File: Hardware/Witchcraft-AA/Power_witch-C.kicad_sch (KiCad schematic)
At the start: 12 parts, among them J3 Conn_Power_Coax_IBM_hanging_M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, J4 Molex_0015913074, J5 Conn_01x02_Socket, U1 Z1 extreme, U2 LM26420-Q1xx-xxxx

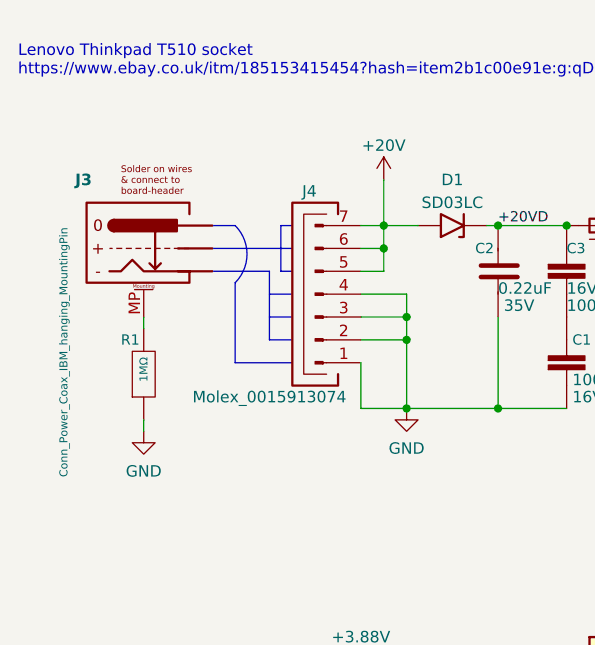
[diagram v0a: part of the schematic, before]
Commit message: Started working on custom buttons for the shell.
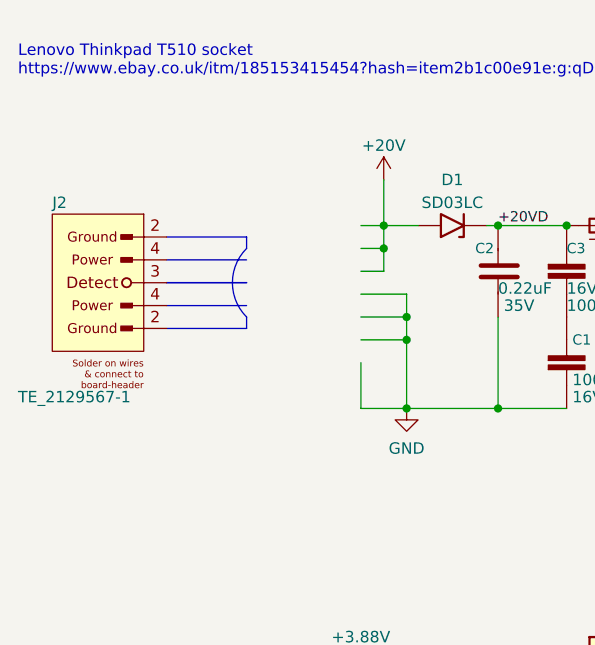
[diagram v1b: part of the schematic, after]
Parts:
- removed J3: Conn_Power_Coax_IBM_hanging_MountingPin, LRJ:Jack_IBM_Coax_Power_5.55x7.5mm_Hanging, symbol LRJ-parts:Conn_Power_Coax_hanging_MountingPin
- removed J4: Molex_0015913074, LRJ:Molex_70634_15913074_1x07-2MP_P2.54mm_Vertical, symbol LRJ-parts:Molex_0015913074
- removed R1: R_ERJ-3GEYJ105V, Resistor_SMD:R_0603_1608Metric, symbol LRJ-parts:R_ERJ-3GEYJ105V
- added J2: TE_2129567-1, LRJ:TE_2129567-1, symbol LRJ-parts:TE_2129567-1

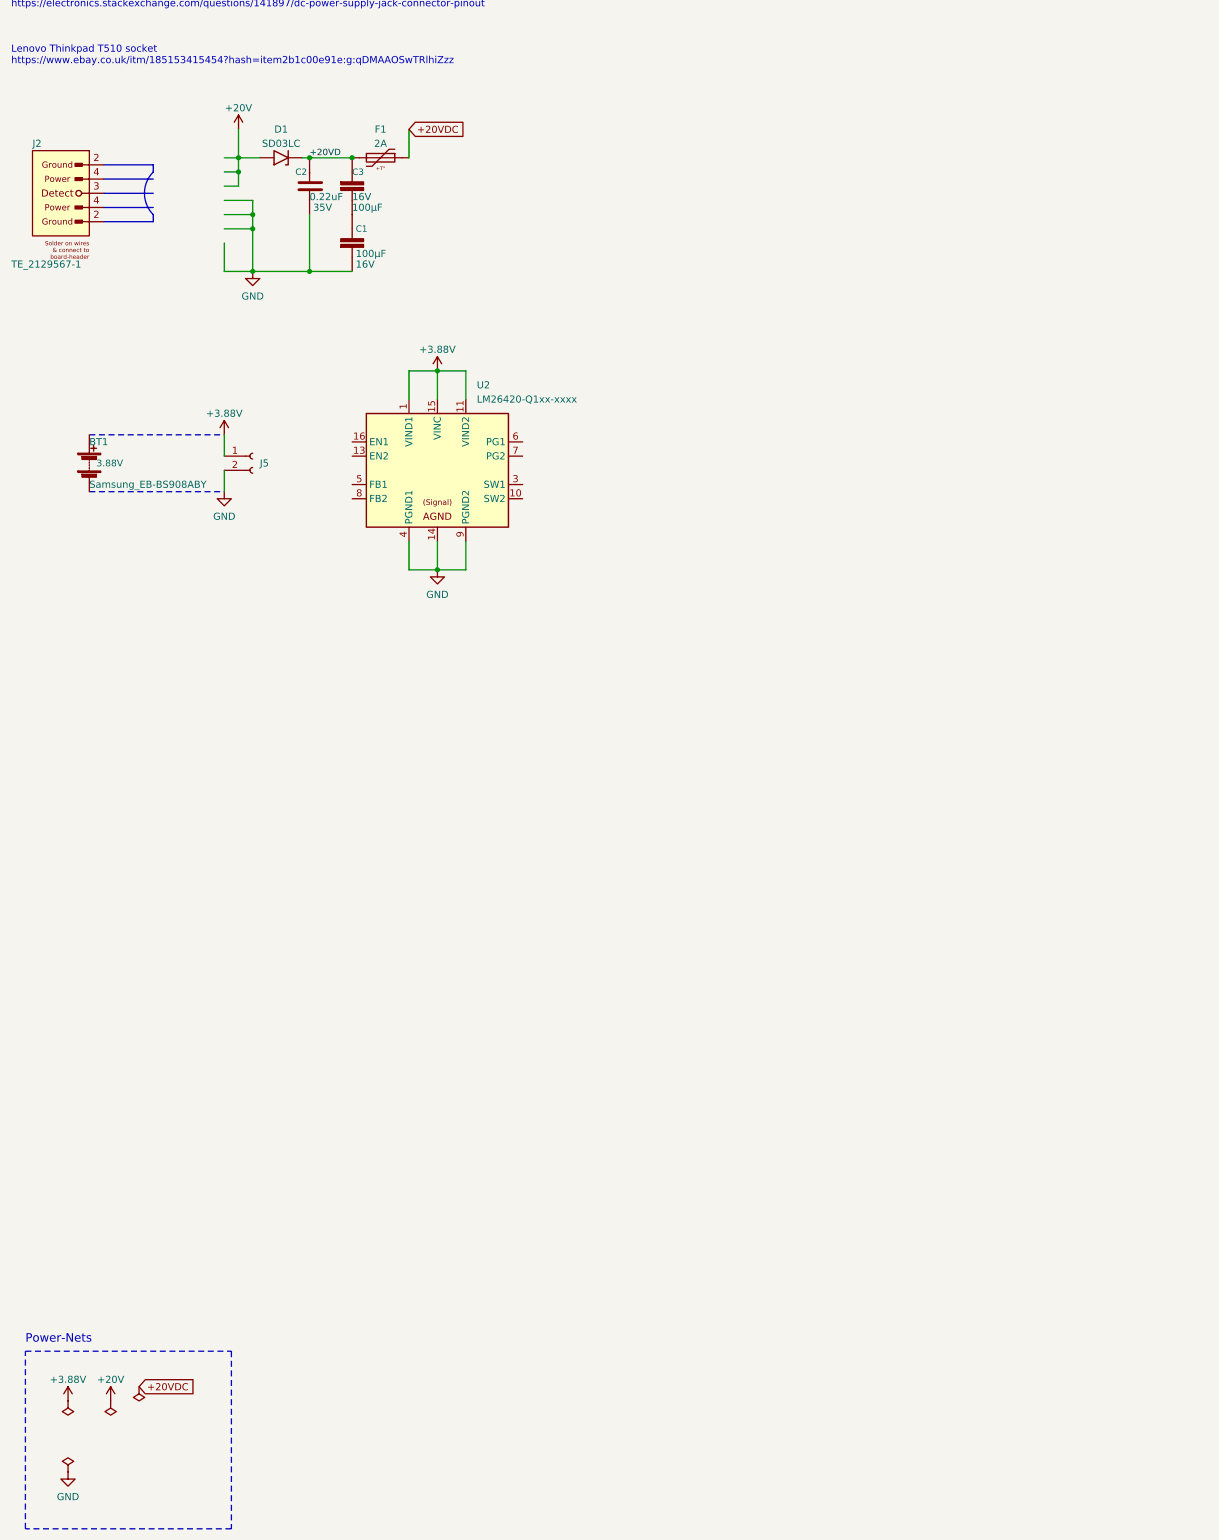
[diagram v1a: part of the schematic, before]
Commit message: added a mag-lev switch assembly to the shell, and started adding button-switches to the schematic.
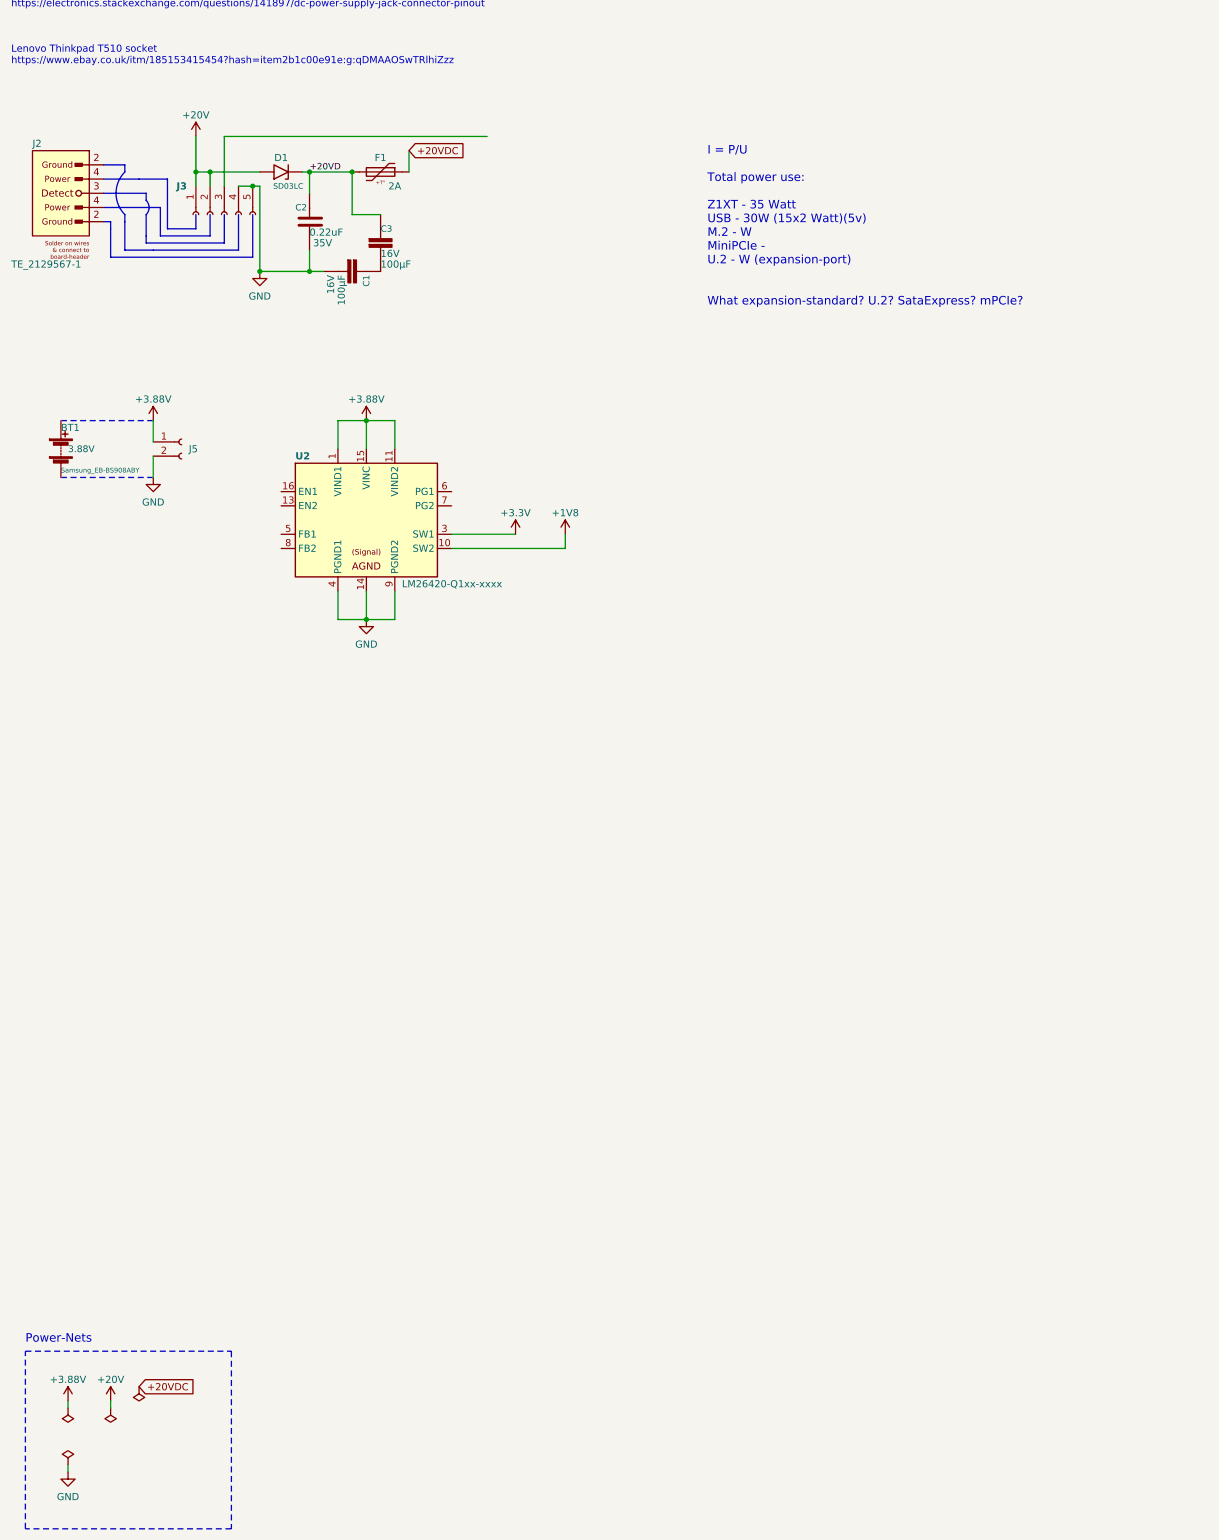
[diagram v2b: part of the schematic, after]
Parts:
- added J3: Conn_01x05_Socket, Connector_PinHeader_1.27mm:PinHeader_1x05_P1.27mm_Vertical_SMD_Pin1Left, symbol Connector:Conn_01x05_Socket
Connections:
- net +20V: now also J3.1 (Pin_1), J3.2 (Pin_2)
- net GND: now also J3.4 (Pin_4), J3.5 (Pin_5)
- net +1V8: now reaches U2.10 (SW2)
- net +3.3V: now reaches U2.3 (SW1)
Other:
- note added: "I = P/U Total power use: Z1XT - 35 Watt USB - 30W (15x2 Watt)(5v) M.2 - W MiniPCIe - U.2 - W (expansion-port) What expansion-standard? U.2? SataExpress? mPCIe?"
- moved on the sheet: BT1, C1, C2, C3, D1, F1, J5, U2

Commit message: Some chances to start/rectangle-buttons in mech, and startedmaking the M.2 ports.
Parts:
- added U3, U4: K3LKCKC0BM, LRJ:SAMSUNG_FBGA-315_12x14mm_Layout23x23_P0.5mmP0.65mm, symbol LRJ-parts:K3LKCKC0BM-MFCP
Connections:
- net GND: now also U3.B12 (VSS), U3.B2 (VSS), U3.B5 (VSS), U3.B6 (VSS), U3.C3 (VSS), U3.C5 (VSS), U3.C6 (VSS), U3.D12 (VSS), U3.D3 (VSS), U3.E4 (VSS), U3.E5 (VSS), U3.E6 (VSS), U3.F12 (VSS), U3.F4 (VSS), U3.F5 (VSS), U3.F6 (VSS), U3.G3 (VSS), U3.G4 (VSS), U3.G6 (VSS), U3.G9 (VSS), U3.H10 (VSS), U3.H2 (VSS), U3.J12 (VSS), U3.J4 (VSS), U3.K10 (VSS), U3.K2 (VSS), U3.L6 (VSS), U3.L9 (VSS), U3.M12 (VSS), U3.M4 (VSS), U3.M5 (VSS), U3.M6 (VSS), U3.N4 (VSS), U3.N5 (VSS), U3.N6 (VSS), U3.P12 (VSS), U3.P3 (VSS), U3.R4 (VSS), U3.R5 (VSS), U3.R6 (VSS), U3.T12 (VSS), U3.T2 (VSS), U3.T3 (VSS), U3.T4 (VSS), U3.T5 (VSS), U3.T6 (VSS), U4.B12 (VSS), U4.B2 (VSS), U4.B5 (VSS), U4.B6 (VSS), U4.C3 (VSS), U4.C5 (VSS), U4.C6 (VSS), U4.D12 (VSS), U4.D3 (VSS), U4.E4 (VSS), U4.E5 (VSS), U4.E6 (VSS), U4.F12 (VSS), U4.F4 (VSS), U4.F5 (VSS), U4.F6 (VSS), U4.G3 (VSS), U4.G4 (VSS), U4.G6 (VSS), U4.G9 (VSS), U4.H10 (VSS), U4.H2 (VSS), U4.J12 (VSS), U4.J4 (VSS), U4.K10 (VSS), U4.K2 (VSS), U4.L6 (VSS), U4.L9 (VSS), U4.M12 (VSS), U4.M4 (VSS), U4.M5 (VSS), U4.M6 (VSS), U4.N4 (VSS), U4.N5 (VSS), U4.N6 (VSS), U4.P12 (VSS), U4.P3 (VSS), U4.R4 (VSS), U4.R5 (VSS), U4.R6 (VSS), U4.T12 (VSS), U4.T2 (VSS), U4.T3 (VSS), U4.T4 (VSS), U4.T5 (VSS), U4.T6 (VSS)
- net Power_Detect: now reaches J3.3 (Pin_3)
- new net: U4.A10 (VDD1), U4.A3 (VDD1), U4.A4 (VDD1), U4.A5 (VDD1), U4.A6 (VDD1), U4.U10 (VDD1), U4.U3 (VDD1), U4.U4 (VDD1), U4.U5 (VDD1), U4.U6 (VDD1)
- new net: U4.A11 (VDDQ), U4.C12 (VDDQ), U4.E12 (VDDQ), U4.E8 (VDDQ), U4.G12 (VDDQ), U4.H11 (VDDQ), U4.H8 (VDDQ), U4.H9 (VDDQ), U4.J10 (VDDQ), U4.J9 (VDDQ), U4.K11 (VDDQ), U4.K8 (VDDQ), U4.L12 (VDDQ), U4.N12 (VDDQ), U4.N8 (VDDQ), U4.R12 (VDDQ), U4.U11 (VDDQ)
- new net: U4.A8 (VDD2), U4.A9 (VDD2), U4.D4 (VDD2), U4.D5 (VDD2), U4.D6 (VDD2), U4.G5 (VDD2), U4.H12 (VDD2), U4.H5 (VDD2), U4.H6 (VDD2), U4.J5 (VDD2), U4.J6 (VDD2), U4.K12 (VDD2), U4.K5 (VDD2), U4.K6 (VDD2), U4.L5 (VDD2), U4.P4 (VDD2), U4.P5 (VDD2), U4.P6 (VDD2), U4.U8 (VDD2), U4.U9 (VDD2)
- new net: U4.F2 (VDDCA), U4.G2 (VDDCA), U4.H3 (VDDCA), U4.L2 (VDDCA), U4.M2 (VDDCA)
- new net: U3.A10 (VDD1), U3.A3 (VDD1), U3.A4 (VDD1), U3.A5 (VDD1), U3.A6 (VDD1), U3.U10 (VDD1), U3.U3 (VDD1), U3.U4 (VDD1), U3.U5 (VDD1), U3.U6 (VDD1)
- new net: U3.A11 (VDDQ), U3.C12 (VDDQ), U3.E12 (VDDQ), U3.E8 (VDDQ), U3.G12 (VDDQ), U3.H11 (VDDQ), U3.H8 (VDDQ), U3.H9 (VDDQ), U3.J10 (VDDQ), U3.J9 (VDDQ), U3.K11 (VDDQ), U3.K8 (VDDQ), U3.L12 (VDDQ), U3.N12 (VDDQ), U3.N8 (VDDQ), U3.R12 (VDDQ), U3.U11 (VDDQ)
- new net: U3.A8 (VDD2), U3.A9 (VDD2), U3.D4 (VDD2), U3.D5 (VDD2), U3.D6 (VDD2), U3.G5 (VDD2), U3.H12 (VDD2), U3.H5 (VDD2), U3.H6 (VDD2), U3.J5 (VDD2), U3.J6 (VDD2), U3.K12 (VDD2), U3.K5 (VDD2), U3.K6 (VDD2), U3.L5 (VDD2), U3.P4 (VDD2), U3.P5 (VDD2), U3.P6 (VDD2), U3.U8 (VDD2), U3.U9 (VDD2)
- new net: U3.F2 (VDDCA), U3.G2 (VDDCA), U3.H3 (VDDCA), U3.L2 (VDDCA), U3.M2 (VDDCA)

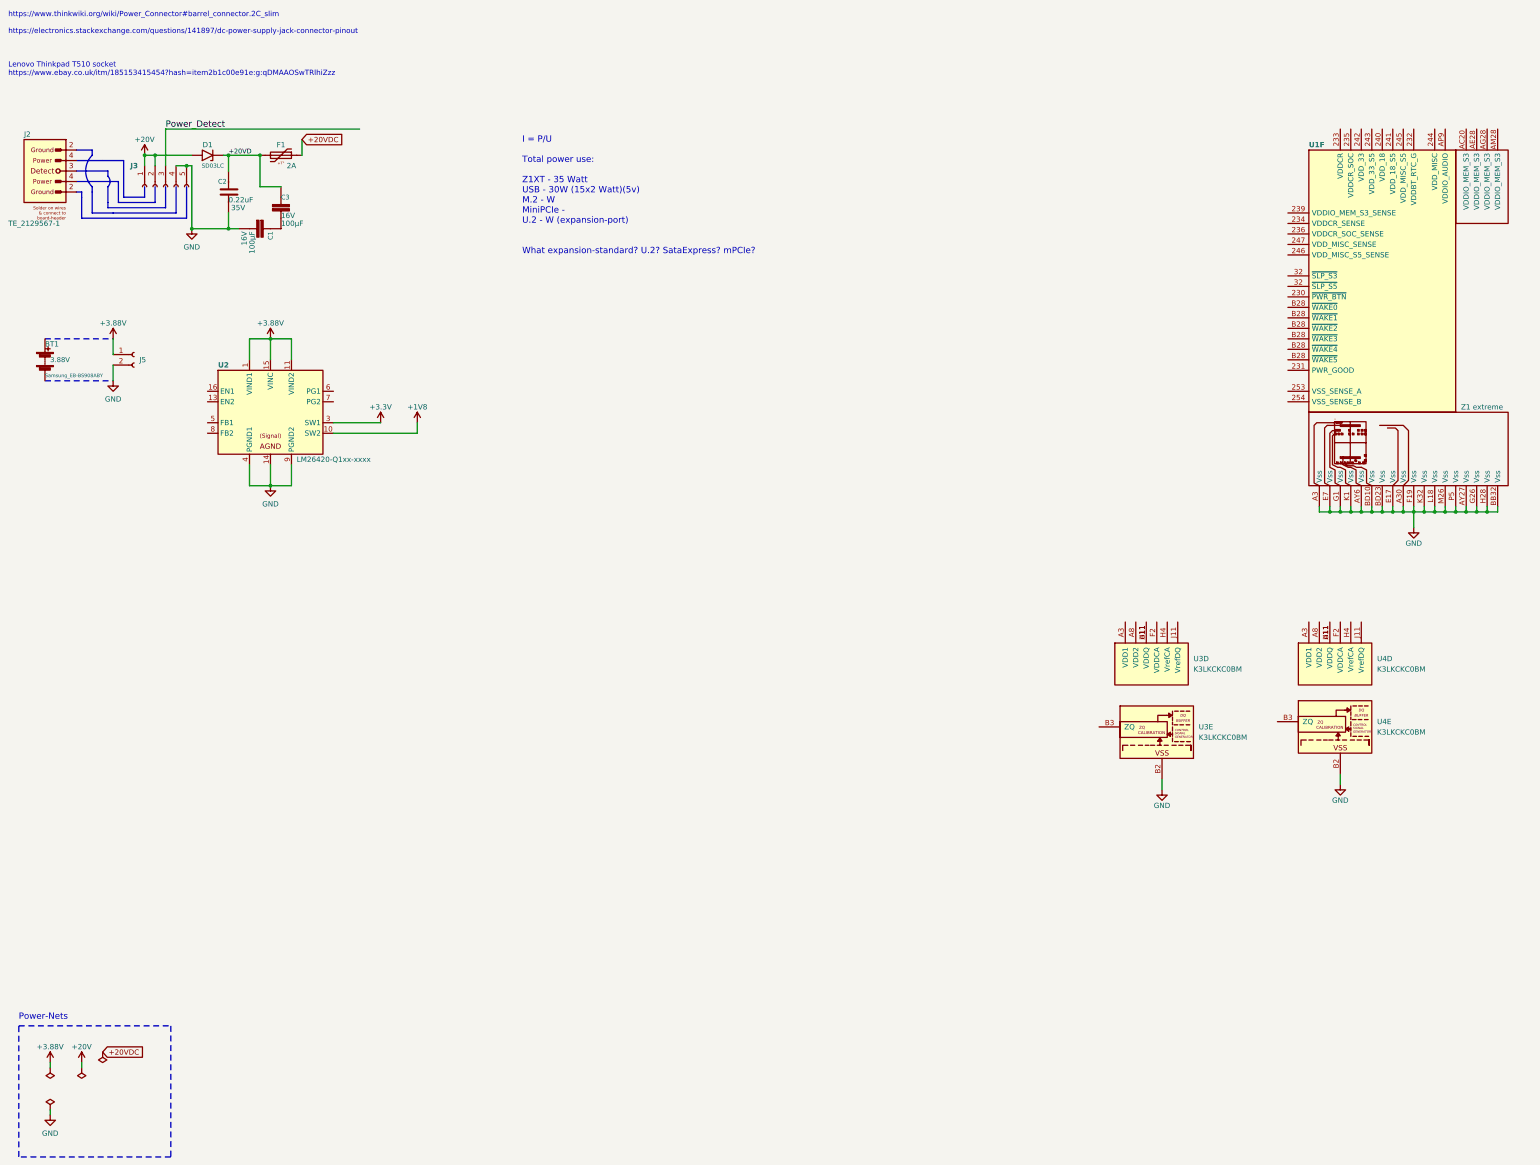
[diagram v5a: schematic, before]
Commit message: Almost completed the design of the new finstack, and have begun work on a redesign of cold-plate and rearrangement of components
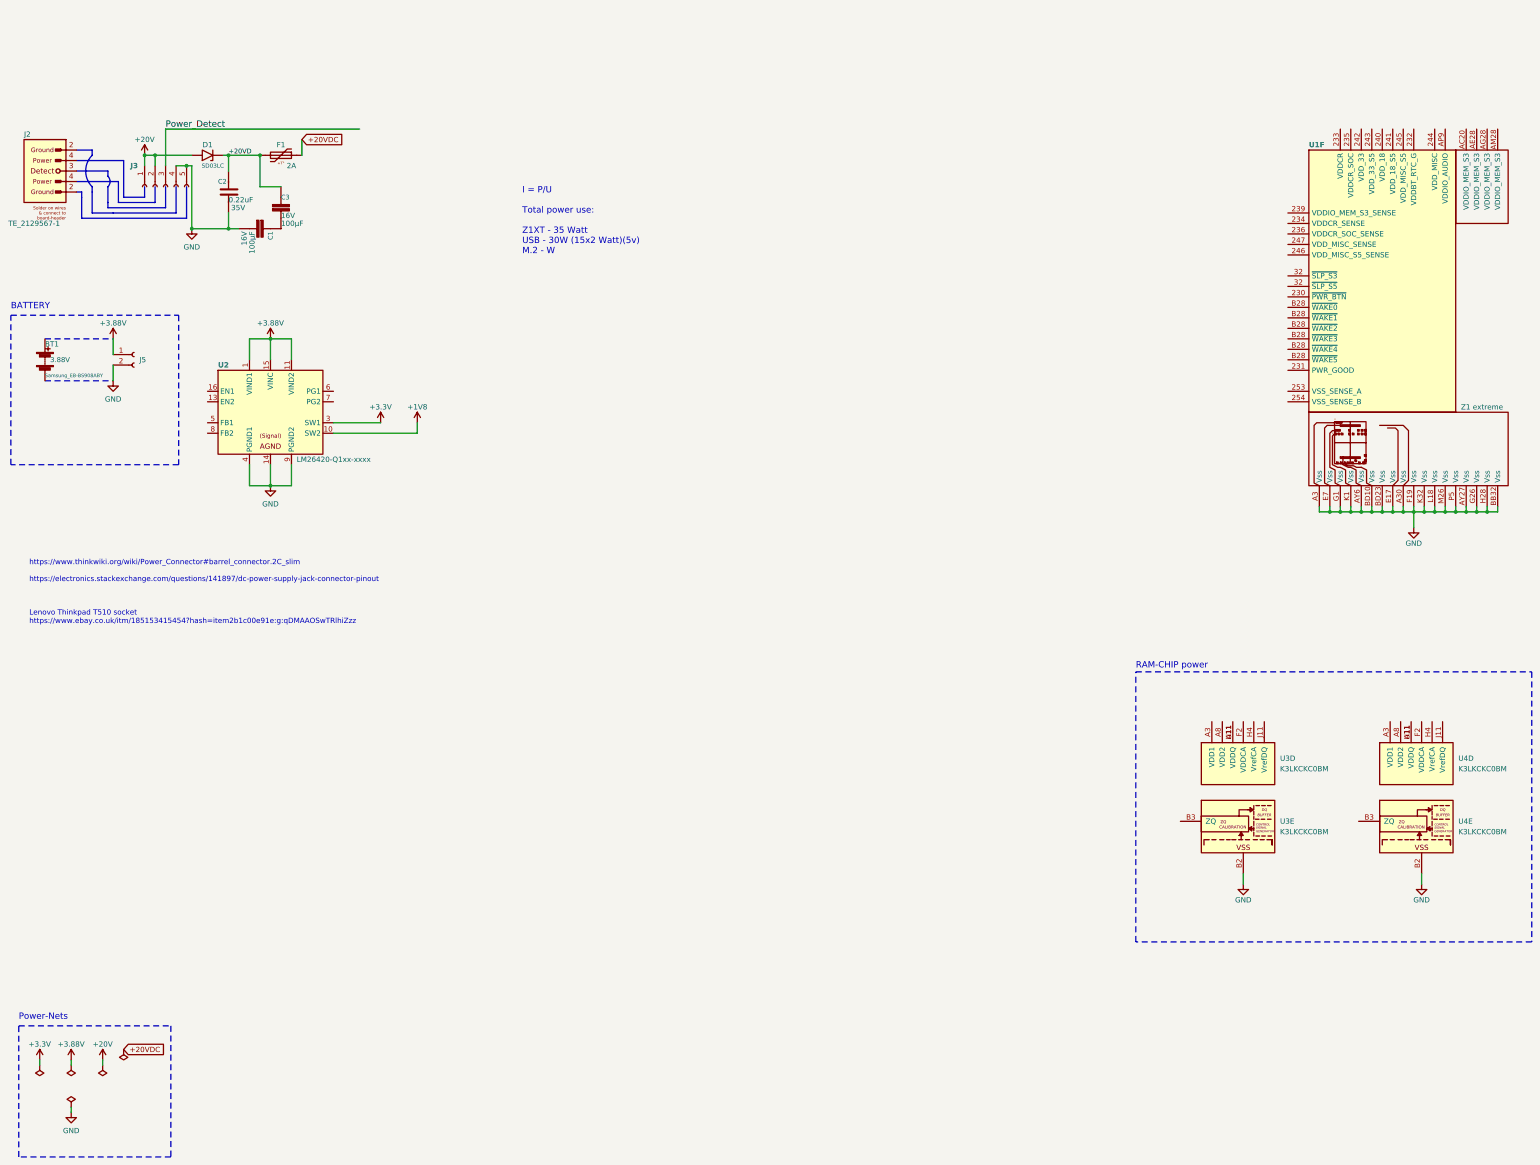
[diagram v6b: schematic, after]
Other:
- note added: "BATTERY"
- note added: "I = P/U Total power use: Z1XT - 35 Watt USB - 30W (15x2 Watt)(5v) M.2 - W"
- note added: "RAM-CHIP power"
- note removed: "I = P/U Total power use: Z1XT - 35 Watt USB - 30W (15x2 Watt)(5v) M.2 - W MiniPCIe - U.2 - W (expansion-port) What expansion-standard? U.2? SataExpress? mPCIe?"
- moved on the sheet: U3D, U3E, U4D, U4E

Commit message: Added the first custom pattern to the casing - Hekate's Wheel.
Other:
- note added: "https://es.aliexpress.com/item/1005005545164108.html?algo_pvid=611ea406-e873-4d66-b3fe-c748b215238d&algo_exp_id=611ea406-e873-4d66-b3fe-c748b215238d-36&pdp_npi=3%40dis%21EUR%211.85%211.77%21%21%21%21%21%40211be3d216886730556973133d07dd%2112000033482130728%21sea%21ES%210&curPageLogUid=Ondxx5G84bRY Possibly Hirose"
- note removed: "Lenovo Thinkpad T510 socket https://www.ebay.co.uk/itm/185153415454?hash=item2b1c00e91e:g:qDMAAOSwTRlhiZzz"
- note removed: "https://www.thinkwiki.org/wiki/Power_Connector#barrel_connector.2C_slim https://electronics.stackexchange.com/questions/141897/dc-power-supply-jack-connector-pinout"
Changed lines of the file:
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@@
     (effects (font (size 1.524 1.524)) (justify left bottom))
-  )
-  (text "https://www.thinkwiki.org/wiki/Power_Connector#barrel_connector.2C_slim\n\nhttps://electronics.stackexchange.com/questions/141897/dc-power-supply-jack-connector-pinout"
-    (at 21.59 140.335 0)
-    (effects (font (size 1.27 1.27)) (justify left bottom))
   )
   (text "BATTERY" (at 17.145 74.295 0)
     (effects (font (size 1.524 1.524)) (justify left bottom))
   )
-  (text "Lenovo Thinkpad T510 socket\nhttps://www.ebay.co.uk/itm/185153415454?hash=item2b1c00e91e:g:qDMAAOSwTRlhiZzz"
-    (at 21.59 150.495 0)
-    (effects (font (size 1.27 1.27)) (justify left bottom))
+  (text "https://es.aliexpress.com/item/1005005545164108.html?algo_pvid=611ea406-e873-4d66-b3fe-c748b215238d&algo_exp_id=611ea406-e873-4d66-b3fe-c748b215238d-36&pdp_npi=3%40dis%21EUR%211.85%211.77%21%21%21%21%21%40211be3d216886730556973133d07dd%2112000033482130728%21sea%21ES%210&curPageLogUid=Ondxx5G84bRY\nPossibly Hirose"
+    (at 14.605 126.365 0)
+    (effects (font (size 1.524 1.524)) (justify left bottom))
   )
   (label "+20VD" (at 69.85 36.83 0) (fields_autoplaced)
